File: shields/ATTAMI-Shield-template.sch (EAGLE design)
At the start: 5 parts

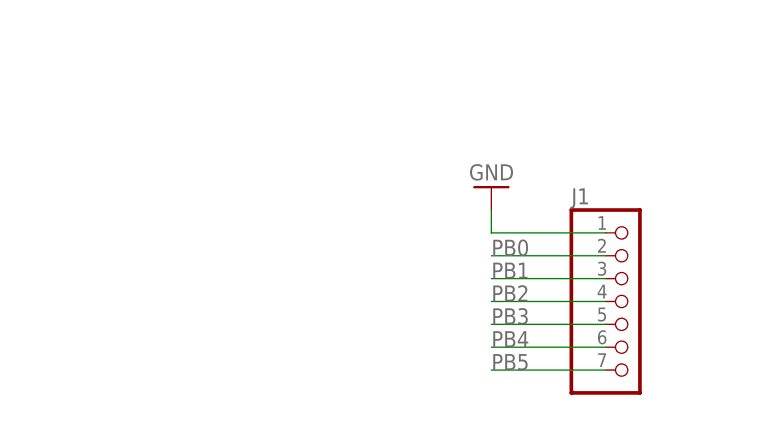
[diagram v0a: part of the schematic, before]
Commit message: added pin number on breakout header
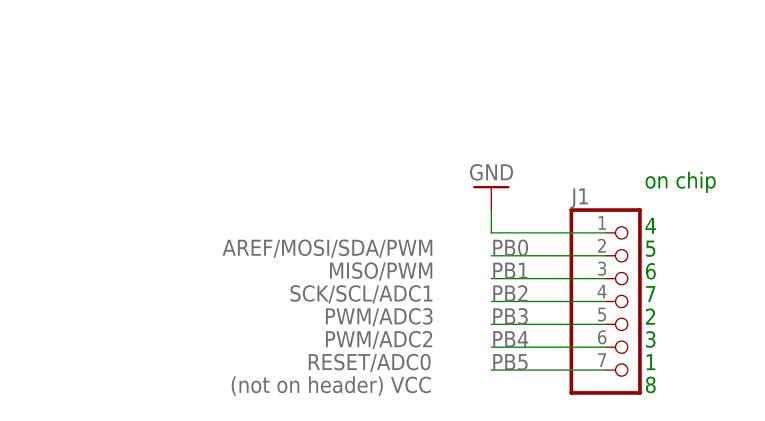
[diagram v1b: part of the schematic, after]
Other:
- note added: "(not on header) VCC"
- note added: "AREF/MOSI/SDA/PWM"
- note added: "MISO/PWM"
- note added: "PWM/ADC2"
- note added: "PWM/ADC3"
- note added: "RESET/ADC0"
- note added: "SCK/SCL/ADC1"
- note added: "on chip 4 5 6 7 2 3 1 8"
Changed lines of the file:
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@@
 <layer number="54" name="bGND_GNDA" color="1" fill="9" visible="no" active="no"/>
 <layer number="56" name="wert" color="7" fill="1" visible="no" active="no"/>
+<layer number="90" name="Modules" color="5" fill="1" visible="yes" active="yes"/>
 <layer number="91" name="Nets" color="2" fill="1" visible="yes" active="yes"/>
 <layer number="92" name="Busses" color="1" fill="1" visible="yes" active="yes"/>
@@
 <text x="59.944" y="144.272" size="1.778" layer="91">VCC (output)</text>
 <text x="18.034" y="144.272" size="1.778" layer="91">V_BAT (input)</text>
+<text x="211.836" y="114.3" size="1.778" layer="95" align="bottom-right">RESET/ADC0</text>
+<text x="212.09" y="119.38" size="1.778" layer="95" font="vector" align="bottom-right">PWM/ADC3</text>
+<text x="212.09" y="121.92" size="1.778" layer="95" align="bottom-right">SCK/SCL/ADC1</text>
+<text x="212.09" y="116.84" size="1.778" layer="95" font="vector" align="bottom-right">PWM/ADC2</text>
+<text x="212.09" y="124.46" size="1.778" layer="95" align="bottom-right">MISO/PWM</text>
+<text x="212.09" y="127" size="1.778" layer="95" align="bottom-right">AREF/MOSI/SDA/PWM</text>
+<text x="235.458" y="111.76" size="1.778" layer="91" distance="42">on chip
+4
+5
+6
+7
+2
+3
+1
+8</text>
+<text x="211.836" y="111.76" size="1.778" layer="95" align="bottom-right">(not on header) VCC</text>
 </plain>
 <instances>

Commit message: updated shield tamplete to only use ATtami lib parts
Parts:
- J1: device microbuilder:HEADER-1X7ROUND -> ATtami:HEADER-1X7ROUND
- J2, J3: device microbuilder:HEADER-1X2ROUND -> ATtami:HEADER-1X2ROUND
- U$1, U$2: device microbuilder:MOUNTINGHOLE2.0 -> ATtami:MOUNTINGHOLE2.0
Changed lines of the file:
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@@
 </classes>
 <parts>
-<part name="GND16" library="SparkFun" deviceset="GND" device=""/>
-<part name="GND1" library="SparkFun" deviceset="GND" device=""/>
-<part name="U$1" library="microbuilder" deviceset="MOUNTINGHOLE" device="2.0" value="MOUNTINGHOLE2.0"/>
-<part name="U$2" library="microbuilder" deviceset="MOUNTINGHOLE" device="2.0" value="MOUNTINGHOLE2.0"/>
-<part name="J2" library="microbuilder" deviceset="HEADER-1X2" device="ROUND"/>
-<part name="J3" library="microbuilder" deviceset="HEADER-1X2" device="ROUND"/>
-<part name="FRAME1" library="frames" deviceset="A4L-LOC" device=""/>
-<part name="J1" library="microbuilder" deviceset="HEADER-1X7" device="ROUND"/>
-<part name="GND5" library="SparkFun" deviceset="GND" device=""/>
+<part name="GND16" library="ATtami" deviceset="GND" device=""/>
+<part name="GND1" library="ATtami" deviceset="GND" device=""/>
+<part name="U$1" library="ATtami" deviceset="MOUNTINGHOLE" device="2.0" value="MOUNTINGHOLE2.0"/>
+<part name="U$2" library="ATtami" deviceset="MOUNTINGHOLE" device="2.0" value="MOUNTINGHOLE2.0"/>
+<part name="J2" library="ATtami" deviceset="HEADER-1X2" device="ROUND"/>
+<part name="J3" library="ATtami" deviceset="HEADER-1X2" device="ROUND"/>
+<part name="FRAME1" library="ATtami" deviceset="A4L-LOC" device=""/>
+<part name="J1" library="ATtami" deviceset="HEADER-1X7" device="ROUND"/>
+<part name="GND5" library="ATtami" deviceset="GND" device=""/>
 </parts>
 <sheets>
